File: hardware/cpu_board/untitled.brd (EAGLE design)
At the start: 126.3 x 94.6 mm, 71 parts, among them IC1 MAX232ECWE, IC2 MAX232ECWE, IC3 AM29F040J, IC4 74HCT138D, IC5 LM2596S, J2 POWER_JACKSLT, U1 AS6C4008-55SIN

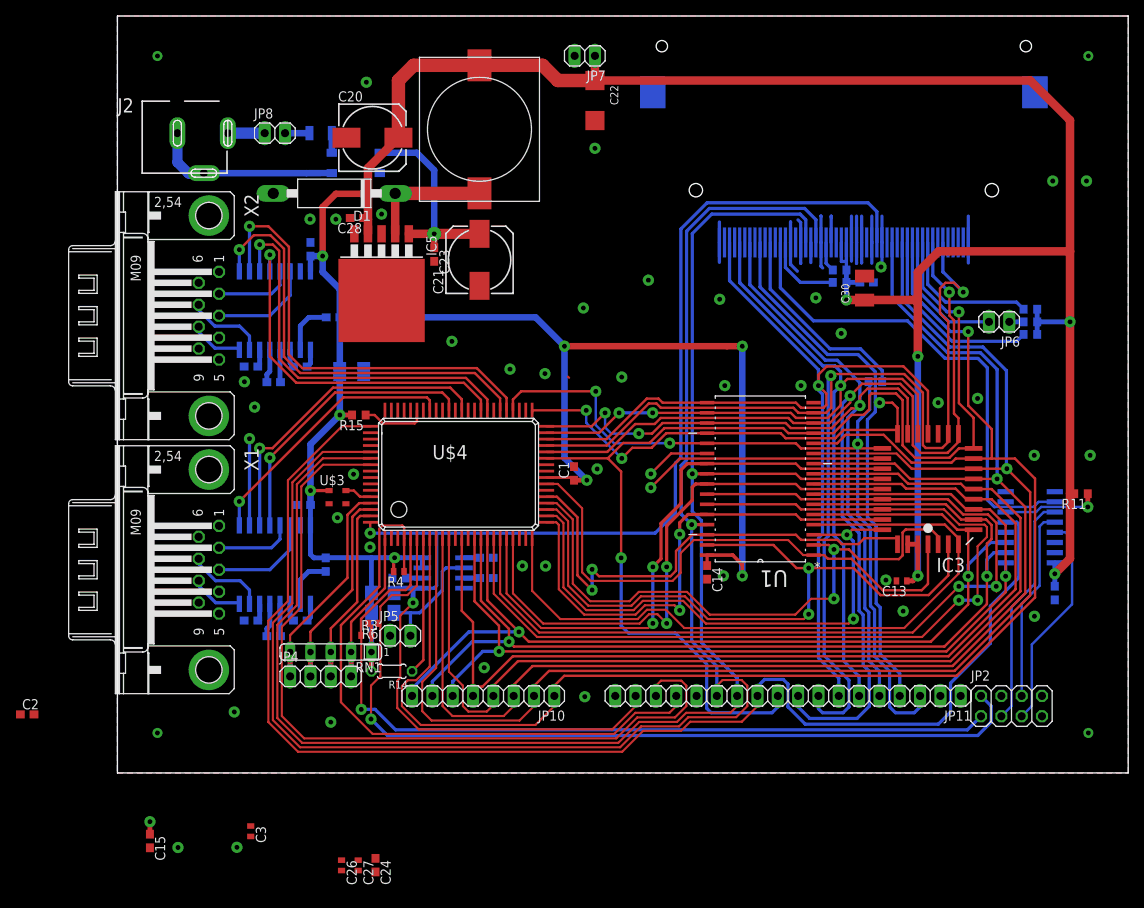
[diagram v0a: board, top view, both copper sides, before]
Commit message: Local port added
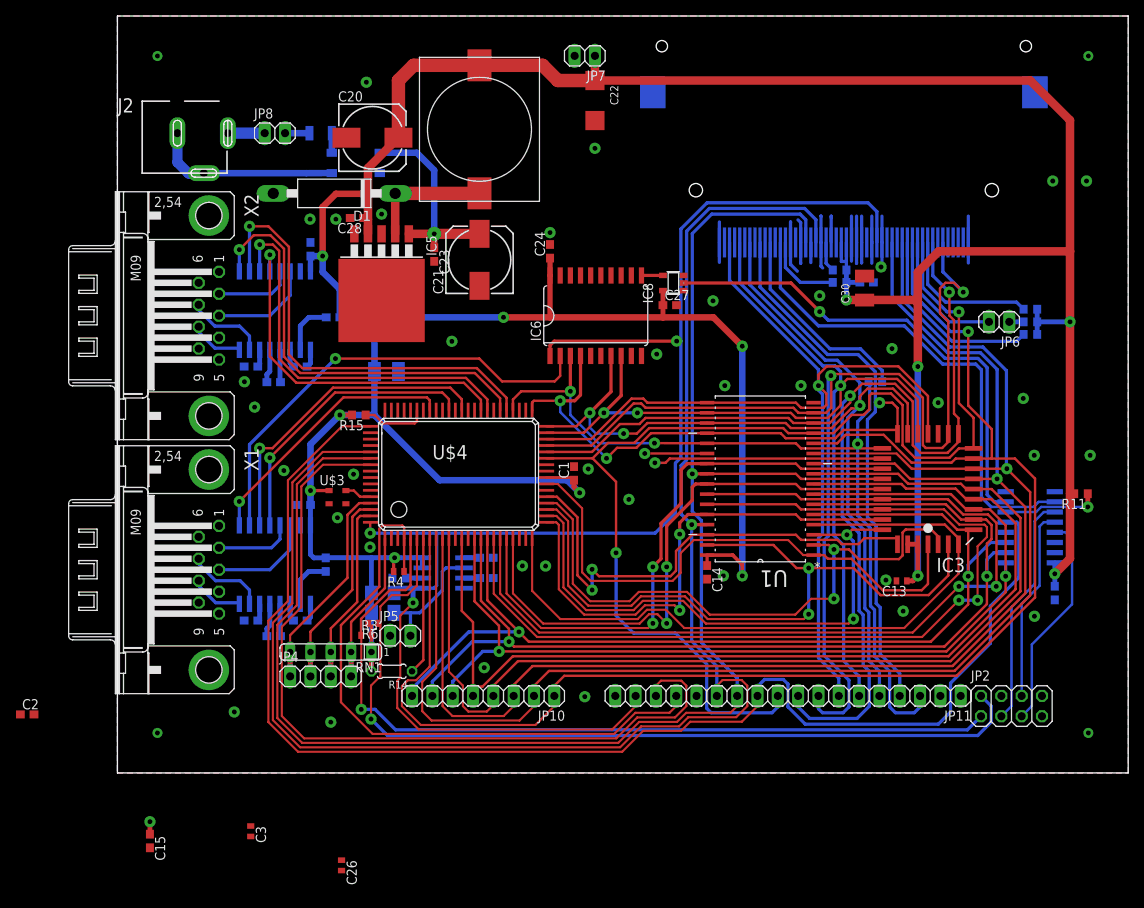
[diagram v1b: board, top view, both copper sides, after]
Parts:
- added IC6: 74HCT273DW, 74xx-eu:SO20W
- added IC8: 74LVC1G04DBV, 74xx-little-us:SOT23-5
- C27: device rcl:C0402 -> rcl:C0603
- moved C27 80.1 mm to (69.0, 58.5), turned to 0 degrees
- moved C24 79.8 mm to (54.1, 65.2), turned to 90 degrees
- moved C31 4.34 mm to (33.6, 50.2)
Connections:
- removed net CS7_NO_USE: IC4.7
- new net LOCAL_PORT_CS: IC4.7, IC8.2
- new net N$44: IC6.11, IC8.4
- net !RST: now also IC6.1
- net 5V: now also IC6.20, IC8.5
- net D4: now also IC6.8
- net D5: now also IC6.7
- net D6: now also IC6.4
- net D7: now also IC6.3
- net GND: now also IC6.10, IC6.13, IC6.14, IC6.17, IC6.18, IC8.3
- net RTS2: now also IC6.2
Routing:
- net LOCAL_PORT_CS: track 0.00 -> 60.9 mm, vias 0 -> 1
- net RTS2: track 10.8 -> 57.3 mm
- net 5V: track 476.4 -> 503.6 mm
- net !RST: track 168.0 -> 185.9 mm, vias 2 -> 3
- net D6: track 125.2 -> 134.4 mm
- net D5: track 122.0 -> 129.8 mm
- net D4: track 121.3 -> 129.0 mm
- net D7: track 102.7 -> 106.4 mm
- net N$44: track 0.00 -> 2.69 mm
- net !ROM_CS: track 30.5 -> 28.7 mm
- net GND: track 65.0 -> 64.8 mm, vias 41 -> 38

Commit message: E signal routed to edge connector
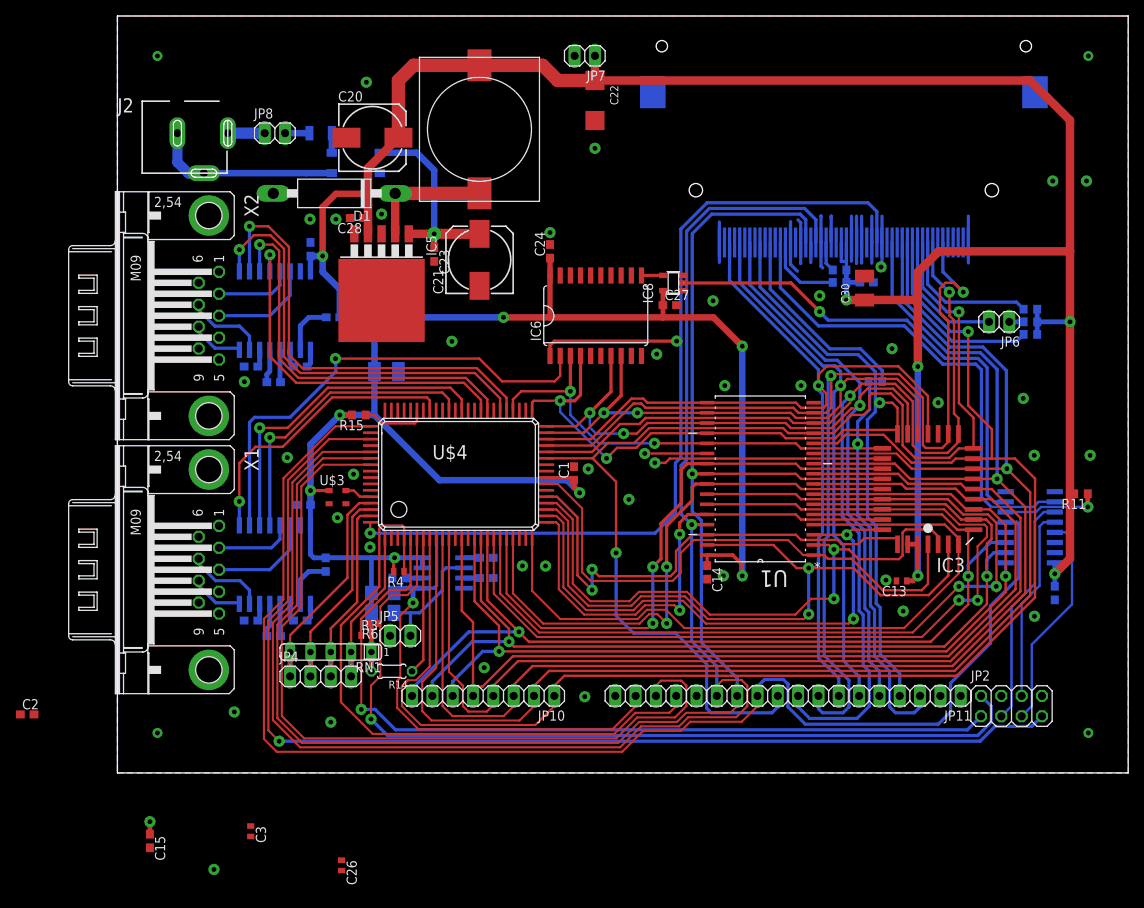
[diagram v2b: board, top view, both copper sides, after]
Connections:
- new net E: JP2.7, U$4.67
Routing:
- net E: track 0.00 -> 143.3 mm, vias 0 -> 1
- net CTS2: track 33.6 -> 36.4 mm
- net RTS2: track 57.3 -> 60.0 mm
- net !IORQ: track 169.7 -> 172.2 mm
- net TXD2: track 40.0 -> 41.5 mm
- net RXD2: track 36.0 -> 37.5 mm
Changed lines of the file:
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@@
 <contactref element="C12" pad="2"/>
 <contactref element="C11" pad="2"/>
-<via x="17.145" y="45.72" extent="1-16" drill="0.6" diameter="1.4224" shape="octagon"/>
+<via x="12.065" y="-12.065" extent="1-16" drill="0.6" diameter="1.4224" shape="octagon"/>
 <via x="24.0792" y="69.215" extent="1-16" drill="0.6" diameter="1.4224" shape="octagon"/>
 <via x="15.875" y="48.895" extent="1-16" drill="0.6" diameter="1.4224" shape="octagon"/>
@@
 <contactref element="IC6" pad="18"/>
 <via x="63.9318" y="34.1884" extent="1-16" drill="0.6" diameter="1.4224" shape="octagon"/>
-<via x="20.8026" y="37.7952" extent="1-16" drill="0.6" diameter="1.4224" shape="octagon"/>
+<via x="21.2344" y="39.4208" extent="1-16" drill="0.6" diameter="1.4224" shape="octagon"/>
 <contactref element="IC8" pad="3"/>
 <via x="74.4474" y="59.0042" extent="1-16" drill="0.6" diameter="1.4224" shape="octagon"/>
 <wire x1="16.6624" y1="-7.9398" x2="28.0162" y2="-12.207" width="0" layer="19" extent="1-1"/>
-<wire x1="4.064" y1="-9.359" x2="16.6624" y2="-7.9398" width="0" layer="19" extent="1-1"/>
+<wire x1="12.065" y1="-12.065" x2="16.6624" y2="-7.9398" width="0" layer="19" extent="1-1"/>
+<wire x1="4.064" y1="-9.359" x2="12.065" y2="-12.065" width="0" layer="19" extent="1-1"/>
 <wire x1="14.605" y1="7.62" x2="16.6624" y2="-7.9398" width="0" layer="19" extent="1-1"/>
 <wire x1="-10.4276" y1="7.3152" x2="4.064" y2="-9.359" width="0" layer="19" extent="1-1"/>
@@
 <signal name="TXD2">
 <contactref element="IC1" pad="11"/>
-<wire x1="17.78" y1="30.9372" x2="17.78" y2="40.5892" width="0.4064" layer="16"/>
-<via x="17.78" y="40.5892" extent="1-16" drill="0.6" diameter="1.4224" shape="octagon"/>
+<wire x1="17.78" y1="30.9372" x2="17.78" y2="43.1292" width="0.4064" layer="16"/>
+<via x="17.78" y="43.1292" extent="1-16" drill="0.6" diameter="1.4224" shape="octagon"/>
 <contactref element="U$4" pad="52"/>
-<wire x1="26.9494" y1="48.1584" x2="41.6052" y2="48.1584" width="0.3048" layer="1"/>
+<wire x1="26.3144" y1="48.1584" x2="41.6052" y2="48.1584" width="0.3048" layer="1"/>
 <wire x1="41.6052" y1="48.1584" x2="43.0402" y2="46.7234" width="0.3048" layer="1"/>
 <wire x1="43.0402" y1="45.3254" x2="43.0402" y2="46.7234" width="0.3048" layer="1"/>
-<wire x1="17.78" y1="40.5892" x2="19.3802" y2="40.5892" width="0.3048" layer="1"/>
-<wire x1="26.9494" y1="48.1584" x2="19.3802" y2="40.5892" width="0.3048" layer="1"/>
+<wire x1="17.78" y1="43.1292" x2="21.2852" y2="43.1292" width="0.3048" layer="1"/>
+<wire x1="26.3144" y1="48.1584" x2="21.2852" y2="43.1292" width="0.3048" layer="1"/>
 </signal>
 <signal name="RTS2">
@@
 <via x="27.2542" y="51.7906" extent="1-16" drill="0.6" diameter="1.4224" shape="octagon"/>
 <contactref element="IC6" pad="2"/>
-<wire x1="16.51" y1="30.9372" x2="16.51" y2="41.0464" width="0.4064" layer="16"/>
-<wire x1="27.2542" y1="51.7906" x2="16.51" y2="41.0464" width="0.4064" layer="16"/>
+<wire x1="16.51" y1="30.9372" x2="16.51" y2="43.815" width="0.4064" layer="16"/>
 <wire x1="27.2542" y1="51.7906" x2="45.2374" y2="51.7906" width="0.3048" layer="1"/>
 <wire x1="45.2374" y1="51.7906" x2="48.0822" y2="48.9458" width="0.3048" layer="1"/>
@@
 <wire x1="54.6608" y1="48.9458" x2="55.3466" y2="49.6316" width="0.3048" layer="1"/>
 <wire x1="55.3466" y1="52.1208" x2="55.3466" y2="49.6316" width="0.3048" layer="1"/>
+<wire x1="16.51" y1="43.815" x2="17.145" y2="44.45" width="0.4064" layer="16"/>
+<wire x1="17.145" y1="44.45" x2="21.59" y2="44.45" width="0.4064" layer="16"/>
+<wire x1="21.59" y1="44.45" x2="27.305" y2="50.165" width="0.4064" layer="16"/>
+<wire x1="27.305" y1="50.165" x2="27.305" y2="51.7398" width="0.4064" layer="16"/>
+<wire x1="27.305" y1="51.7398" x2="27.2542" y2="51.7906" width="0.4064" layer="16"/>
 </signal>
 <signal name="RXD2">
 <contactref element="IC1" pad="12"/>
-<wire x1="19.05" y1="30.9372" x2="19.05" y2="39.3954" width="0.4064" layer="16"/>
-<via x="19.05" y="39.3954" extent="1-16" drill="0.6" diameter="1.4224" shape="octagon"/>
+<wire x1="19.05" y1="30.9372" x2="19.05" y2="41.9354" width="0.4064" layer="16"/>
+<via x="19.05" y="41.9354" extent="1-16" drill="0.6" diameter="1.4224" shape="octagon"/>
 <contactref element="U$4" pad="54"/>
-<wire x1="27.2034" y1="47.5488" x2="40.6146" y2="47.5488" width="0.3048" layer="1"/>
+<wire x1="26.5938" y1="47.5488" x2="40.6146" y2="47.5488" width="0.3048" layer="1"/>
 <wire x1="40.6146" y1="47.5488" x2="41.4402" y2="46.7232" width="0.3048" layer="1"/>
 <wire x1="41.4402" y1="45.3254" x2="41.4402" y2="46.7232" width="0.3048" layer="1"/>
-<wire x1="27.2034" y1="47.5488" x2="19.05" y2="39.3954" width="0.3048" layer="1"/>
+<wire x1="19.05" y1="41.9354" x2="20.9804" y2="41.9354" width="0.3048" layer="1"/>
+<wire x1="26.5938" y1="47.5488" x2="20.9804" y2="41.9354" width="0.3048" layer="1"/>
 </signal>
 <signal name="CTS2">
@@
 <via x="15.24" y="33.9344" extent="1-16" drill="0.6" diameter="1.4224" shape="octagon"/>
 <contactref element="U$4" pad="57"/>
-<wire x1="28.2448" y1="46.9392" x2="38.6842" y2="46.9392" width="0.3048" layer="1"/>
+<wire x1="26.8478" y1="46.9392" x2="38.6842" y2="46.9392" width="0.3048" layer="1"/>
 <wire x1="38.6842" y1="46.9392" x2="39.0402" y2="46.5832" width="0.3048" layer="1"/>
 <wire x1="39.0402" y1="45.3254" x2="39.0402" y2="46.5832" width="0.3048" layer="1"/>
-<wire x1="15.24" y1="33.9344" x2="28.2448" y2="46.9392" width="0.3048" layer="1"/>
+<wire x1="26.8478" y1="46.9392" x2="20.6756" y2="40.767" width="0.3048" layer="1"/>
+<wire x1="20.6756" y1="40.767" x2="17.272" y2="40.767" width="0.3048" layer="1"/>
+<wire x1="15.24" y1="33.9344" x2="15.24" y2="38.735" width="0.3048" layer="1"/>
+<wire x1="15.24" y1="38.735" x2="17.272" y2="40.767" width="0.3048" layer="1"/>
 </signal>
 <signal name="N$20">
@@
 <wire x1="56.6166" y1="44.7548" x2="60.1726" y2="41.1988" width="0.3048" layer="16"/>
 <wire x1="50.4698" y1="47.7012" x2="56.6166" y2="47.7012" width="0.3048" layer="1"/>
-<via x="67.1322" y="41.2242" extent="1-16" drill="0.6" diameter="1.4224" shape="octagon"/>
-<wire x1="73.7108" y1="41.1988" x2="67.1322" y2="41.2242" width="0.3048" layer="1"/>
-<wire x1="67.1322" y1="41.2242" x2="60.1726" y2="41.1988" width="0.3048" layer="16"/>
+<via x="67.1322" y="41.1988" extent="1-16" drill="0.6" diameter="1.4224" shape="octagon"/>
 <contactref element="IC6" pad="3"/>
 <wire x1="56.6166" y1="52.1208" x2="56.6166" y2="47.7012" width="0.4064" layer="1"/>
 <wire x1="56.6166" y1="47.7012" x2="56.6166" y2="44.7548" width="0.3048" layer="16"/>
+<wire x1="73.7108" y1="41.1988" x2="67.1322" y2="41.1988" width="0.3048" layer="1"/>
+<wire x1="67.1322" y1="41.1988" x2="60.1726" y2="41.1988" width="0.3048" layer="16"/>
 </signal>
 <signal name="!IORQ">
 <wire x1="80.01" y1="8.3566" x2="80.01" y2="9.6266" width="0.2667" layer="1"/>
-<wire x1="22.5806" y1="2.6416" x2="63.0936" y2="2.6416" width="0.2667" layer="1"/>
+<wire x1="19.9136" y1="2.6416" x2="63.0936" y2="2.6416" width="0.2667" layer="1"/>
 <contactref element="IC4" pad="5"/>
 <wire x1="80.01" y1="9.6266" x2="80.01" y2="10.795" width="0.4064" layer="16"/>
@@
 <contactref element="JP11" pad="11"/>
 <contactref element="U$4" pad="65"/>
-<wire x1="22.5806" y1="2.6416" x2="18.8722" y2="6.35" width="0.2667" layer="1"/>
-<wire x1="18.8722" y1="6.35" x2="18.8722" y2="19.0246" width="0.2667" layer="1"/>
-<wire x1="18.8722" y1="19.0246" x2="21.3106" y2="21.463" width="0.2667" layer="1"/>
-<wire x1="21.3106" y1="36.576" x2="28.06" y2="43.3254" width="0.2667" layer="1"/>
-<wire x1="31.6402" y1="43.3254" x2="28.06" y2="43.3254" width="0.2667" layer="1"/>
-<wire x1="21.3106" y1="36.576" x2="21.3106" y2="21.463" width="0.2667" layer="1"/>
+<wire x1="31.6402" y1="43.3254" x2="27.2472" y2="43.3254" width="0.2667" layer="1"/>
+<wire x1="27.2472" y1="43.3254" x2="20.7518" y2="36.83" width="0.2667" layer="1"/>
+<wire x1="20.7518" y1="36.83" x2="20.7518" y2="21.6916" width="0.2667" layer="1"/>
+<wire x1="20.7518" y1="21.6916" x2="18.3134" y2="19.2532" width="0.2667" layer="1"/>
+<wire x1="18.3134" y1="19.2532" x2="18.3134" y2="4.2418" width="0.2667" layer="1"/>
+<wire x1="18.3134" y1="4.2418" x2="19.9136" y2="2.6416" width="0.2667" layer="1"/>
 </signal>
 <signal name="!RD">
@@
 <wire x1="70.7844" y1="61.2394" x2="84.201" y2="61.2394" width="0.4064" layer="1"/>
 </signal>
+<signal name="E">
+<contactref element="U$4" pad="67"/>
+<contactref element="JP2" pad="7"/>
+<wire x1="31.6402" y1="41.7254" x2="26.46" y2="41.7254" width="0.2667" layer="1"/>
+<wire x1="26.46" y1="41.7254" x2="21.3106" y2="36.576" width="0.2667" layer="1"/>
+<wire x1="21.3106" y1="36.576" x2="21.3106" y2="21.463" width="0.2667" layer="1"/>
+<wire x1="21.3106" y1="21.463" x2="18.8722" y2="19.0246" width="0.2667" layer="1"/>
+<wire x1="18.8722" y1="19.0246" x2="18.8722" y2="5.3086" width="0.2667" layer="1"/>
+<via x="20.2184" y="3.9624" extent="1-16" drill="0.6" diameter="1.4224" shape="octagon"/>
+<wire x1="20.2184" y1="3.9624" x2="107.8484" y2="3.9624" width="0.4064" layer="16"/>
+<wire x1="107.8484" y1="3.9624" x2="109.7026" y2="5.8166" width="0.4064" layer="16"/>
+<wire x1="109.7026" y1="5.8166" x2="114.3" y2="5.8166" width="0.4064" layer="16"/>
+<wire x1="114.3" y1="5.8166" x2="115.57" y2="7.0866" width="0.4064" layer="16"/>
+<wire x1="18.8722" y1="5.3086" x2="20.2184" y2="3.9624" width="0.2667" layer="1"/>
+</signal>
 </signals>

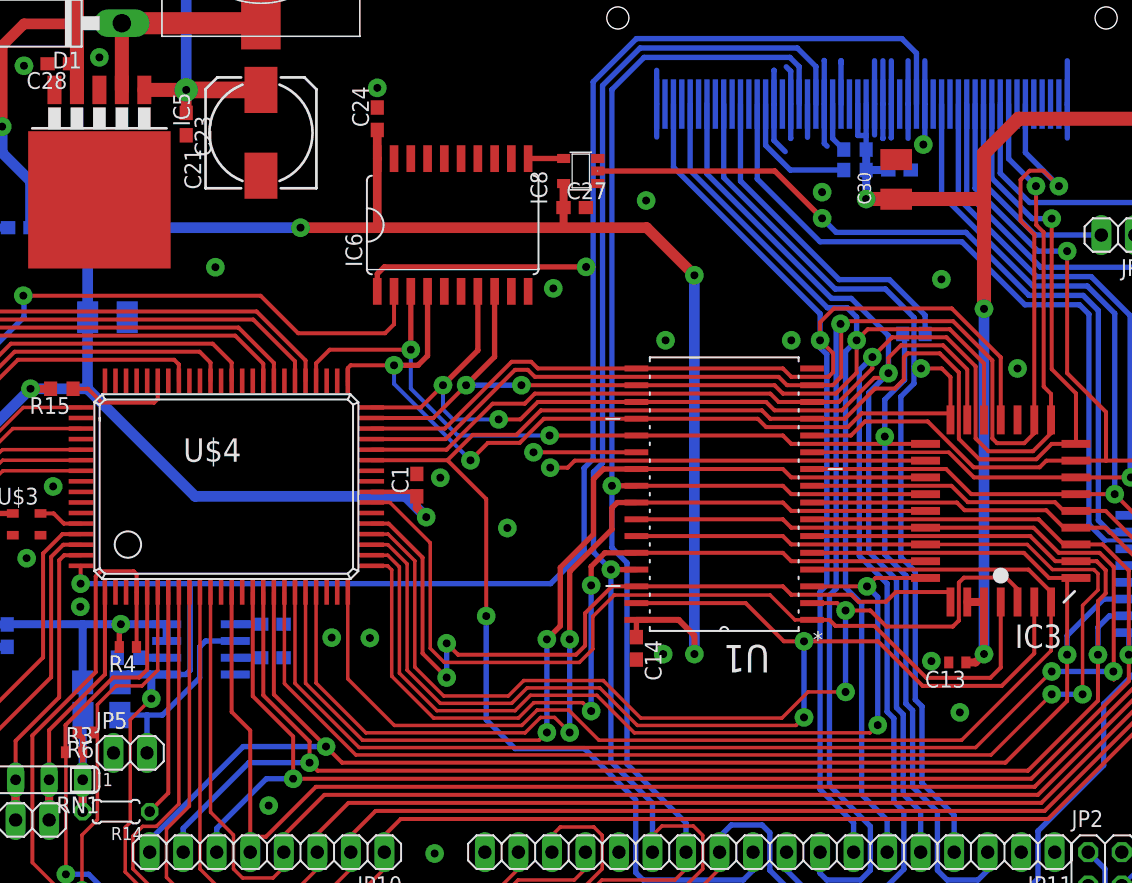
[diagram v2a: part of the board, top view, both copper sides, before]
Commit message: Memory address decoder (work in progress)
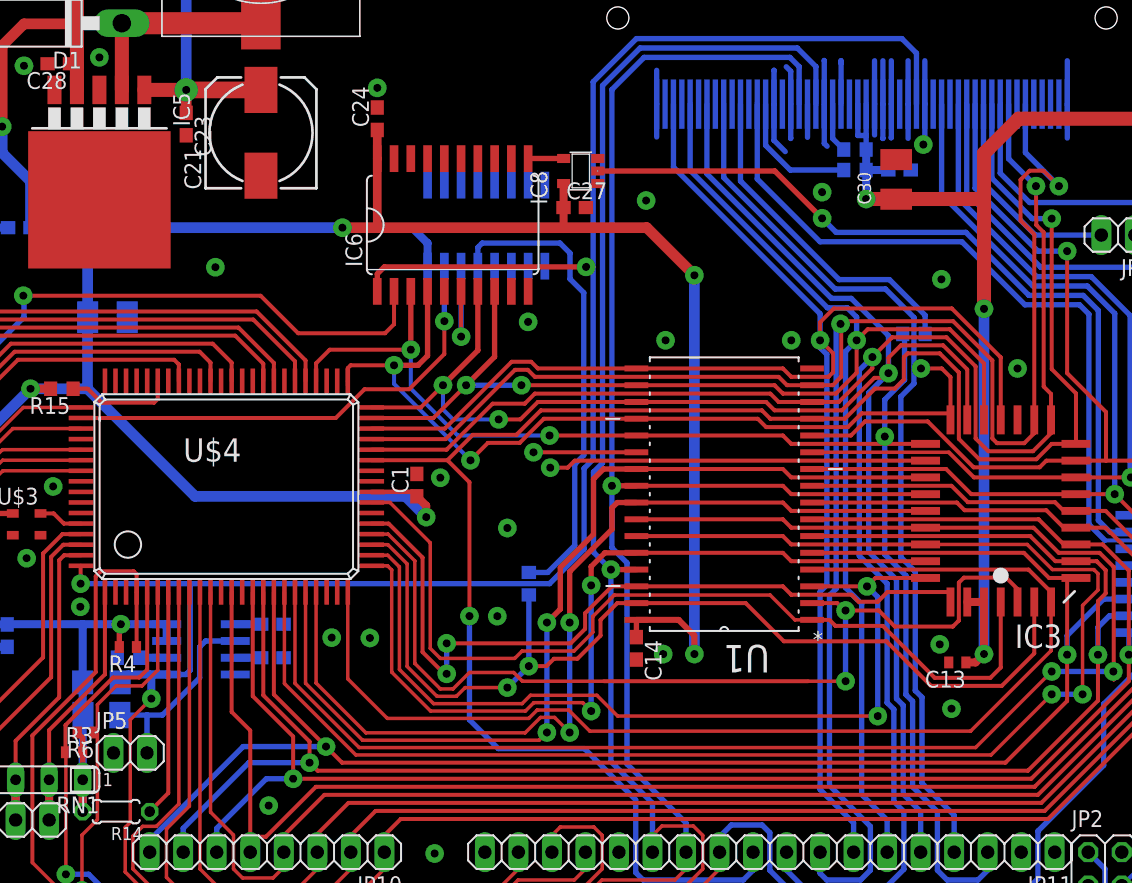
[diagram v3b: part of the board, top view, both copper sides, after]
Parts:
- added IC7: 74HCT139D, 74xx-eu:SO16
- added R16: (no value), rcl:R0603
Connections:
- new net !MEMEN: IC7.15, U$4.66
- new net N$45: IC7.13, R16.2
- new net ROMEN: IC6.6, IC7.14
- net 5V: now also IC7.16
- net A15: now also R16.1
- net GND: now also IC7.1, IC7.2, IC7.3, IC7.8
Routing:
- net !MEMEN: track 0.00 -> 36.2 mm, vias 0 -> 1
- net N$45: track 0.00 -> 36.1 mm
- net A15: track 87.8 -> 76.1 mm
- net ROMEN: track 0.00 -> 8.76 mm, vias 0 -> 1
- net 5V: track 503.6 -> 512.3 mm
- net A16: track 75.2 -> 72.3 mm
- net A14: track 69.6 -> 67.5 mm
- net A17: track 61.7 -> 59.8 mm
- net A12: track 88.8 -> 87.8 mm
- net A18: track 68.8 -> 67.8 mm
- net D0: track 145.3 -> 146.0 mm
- net A13: track 63.9 -> 63.2 mm
- net GND: vias 38 -> 39

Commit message: Minor changes
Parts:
- removed IC7: 74HCT139D, 74xx-eu:SO16
- moved IC6 0.20 mm to (59.8, 56.9)
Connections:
- removed net N$45: IC7.13, R16.2
- removed net ROMEN: IC6.6, IC7.14
- new net ROMSHADOW: IC6.6
- new net _A15: R16.2
- net !MEMEN: no longer IC7.15
- net 5V: no longer IC7.16
- net GND: no longer IC7.1, IC7.2, IC7.3, IC7.8
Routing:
- net _A15: track 0.00 -> 40.6 mm
- net N$45: track 36.1 -> 0.00 mm
- net !ROM_CS: track 28.7 -> 59.5 mm
- net !RAM_CS: track 7.80 -> 38.6 mm
- net ROMSHADOW: track 0.00 -> 21.1 mm, vias 0 -> 1
- net !MEMEN: track 36.2 -> 48.5 mm
- net ROMEN: track 8.76 -> 0.00 mm, vias 1 -> 0
- net 5V: track 512.3 -> 503.6 mm
- net D5: track 129.8 -> 128.5 mm
- net D6: track 134.4 -> 135.6 mm
- net D7: track 106.4 -> 105.6 mm
